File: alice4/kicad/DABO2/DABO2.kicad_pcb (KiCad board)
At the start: 2 copper layers, 74.3 x 117.9 mm, 26 parts, among them J1 POWER, J2 FIRE, J3 HOME, J4 BARTCONN, J5 BLE_DFU, P3 CONN_02X20, P4 CONN_02X07, U1 stmpe811, U2 TFTFRIEND, U3 l3gd20h_breakout, U4 powerboost1000c, U5 bluefruit_le_spi

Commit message: first draft of layout
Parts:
- removed P4: CONN_02X07, DIH_2x7x2mm:DIH_2x7x2mm
- removed REF** (x2): MountingHole_2-5mm, Mounting_Holes:MountingHole_2-5mm
- added C10: 100nF, Capacitors_SMD:C_1206, F.Cu at (171.9, 92.4)
- added C11: 10nF, Capacitors_SMD:C_1206, F.Cu at (168.8, 84.8)
- added C12: 2.2uF, Capacitors_SMD:C_1206, F.Cu at (112.4, 96.6)
- added C13: 100nF, Capacitors_SMD:C_1206, F.Cu at (166.8, 90.3)
- added C14: 100uF, Capacitors_SMD:C_1206, F.Cu at (112.3, 93.6)
- added C15: 10uF, Capacitors_SMD:C_1206, F.Cu at (166.8, 87.9)
- added C16: 10uF, Capacitors_SMD:C_1206, F.Cu at (126.6, 108.2)
- added C17: .1uF, Capacitors_SMD:C_1206, F.Cu at (126.5, 105.7)
- added C18: 10uF, Capacitors_SMD:C_1206, F.Cu at (110.9, 85.0)
- added C6: 10uF, Capacitors_SMD:C_1206, F.Cu at (154.5, 104.9)
- added C7: 1uF, Capacitors_SMD:C_1206, F.Cu at (156.9, 94.1)
- added C8: 1uF, Capacitors_SMD:C_1206, F.Cu at (160.0, 94.1)
- added C9: .1uF, Capacitors_SMD:C_1206, F.Cu at (146.2, 97.9)
- added D1: MBR0540, Diodes_SMD:D_SOD-123, F.Cu at (154.1, 94.3)
- added D2: MM3Z24VT1G, Diodes_SMD:D_SOD-123, F.Cu at (150.3, 97.1)
- added J6: +50mA, Connectors:GS2, B.Cu at (135.1, 97.8)
- added J7: 5VOUT, Pin_Headers:Pin_Header_Straight_1x02_Pitch2.54mm, F.Cu at (107.6, 93.3)
- added J8: PWRSW, Connectors_JST:JST_PH_S2B-PH-SM4-TB_02x2.00mm_Angled, F.Cu at (181.9, 86.4)
- added J9: 5VIN, Pin_Headers:Pin_Header_Straight_1x02_Pitch2.54mm, F.Cu at (107.7, 83.6)
- added L1: 10uH, Resistors_SMD:R_1210, F.Cu at (156.2, 100.9)
- added L2: 6.8uH, Inductors_SMD:L_0402, F.Cu at (119.5, 102.2)
- added R10: 2.2K, Resistors_SMD:R_1206, F.Cu at (173.3, 117.4)
- added R11: 2.2K, Resistors_SMD:R_1206, F.Cu at (173.4, 113.3)
- added R14: 1.87M, Resistors_SMD:R_1206, F.Cu at (121.2, 95.0)
- added R15: 200K, Resistors_SMD:R_1206, F.Cu at (126.4, 95.0)
- added R16: 10K, Resistors_SMD:R_1206, F.Cu at (129.5, 100.5)
- added R17: 10K, Resistors_SMD:R_1206, F.Cu at (172.4, 105.7)
- added R6: 12, Resistors_SMD:R_1206, F.Cu at (140.1, 105.7)
- added R7: 12, Resistors_SMD:R_1206, F.Cu at (140.2, 101.8)
- added R8: 6, Resistors_SMD:R_1206, F.Cu at (140.1, 97.8)
- added R9: 1K, Resistors_SMD:R_1206, F.Cu at (109.9, 100.8)
- added TH1: 15K, Resistors_SMD:R_1206, F.Cu at (169.2, 117.6)
- C1, C2, C3, C4, C5: footprint Capacitors_SMD:C_1206_HandSoldering -> Capacitors_SMD:C_1206
- J1: value POWER -> LIPO; footprint Pin_Headers:Pin_Header_Straight_1x02 -> Connectors_JST:JST_PH_S2B-PH-SM4-TB_02x2.00mm_Angled
- J2: value FIRE -> CONN_01X40; footprint Pin_Headers:Pin_Header_Straight_1x02 -> kyocera_6288:kyocera_6288; moved to B.Cu
- J3: footprint Pin_Headers:Pin_Header_Straight_1x02 -> Connectors_JST:JST_PH_S2B-PH-SM4-TB_02x2.00mm_Angled
- J4: value BARTCONN -> +25mA; footprint Pin_Headers:Pin_Header_Straight_1x05 -> Connectors:GS2; moved to B.Cu
- J5: value BLE_DFU -> +25mA; footprint Pin_Headers:Pin_Header_Straight_1x02 -> Connectors:GS2; moved to B.Cu
- P3: value CONN_02X20 -> GPIO0; footprint Pin_Headers:Pin_Header_Straight_2x20 -> Pin_Headers:Pin_Header_Straight_2x20_Pitch2.54mm; moved to B.Cu
- R1: value 50K -> 10K; footprint Resistors_SMD:R_1206_HandSoldering -> Resistors_SMD:R_1206
- R2: value 10K -> 330K; footprint Resistors_SMD:R_1206_HandSoldering -> Resistors_SMD:R_1206
- R3: value 50K -> 12; footprint Resistors_SMD:R_1206_HandSoldering -> Resistors_SMD:R_1206
- R4: value 10K -> 110K; footprint Resistors_SMD:R_1206_HandSoldering -> Resistors_SMD:R_1206
- R5: value 10K -> 100K; footprint Resistors_SMD:R_1206_HandSoldering -> Resistors_SMD:R_1206
- U2: value TFTFRIEND -> l3gd20h; footprint DIP40:DIP-40_1_ELL -> l3gd20h:l3gd20h
- U3: value l3gd20h_breakout -> mcp73871; footprint L3GD20H:l3gd20h -> Housings_DFN_QFN:QFN-20-1EP_4x4mm_Pitch0.5mm
- U4: value powerboost1000c -> tps61090rsar; footprint PowerBoost1000c:powerboost1000c -> Housings_DFN_QFN:QFN-16-1EP_4x4mm_Pitch0.65mm
- U5: value bluefruit_le_spi -> fan5333bsx; footprint Bluefruit LE SPI:bluefruit_le_spi -> TO_SOT_Packages_SMD:SOT-23-5
- moved J3 88.6 mm to (195.4, 107.5)
- moved HOLE0 73.6 mm to (107.7, 116.4), turned to 270 degrees
- moved U2 69.9 mm to (171.3, 88.1), turned to 90 degrees
- moved P3 62.6 mm to (116.9, 115.5), turned to 270 degrees
- moved HOLE1 57.0 mm to (197.3, 116.4), turned to 270 degrees
- moved U1 56.6 mm to (168.3, 104.0), turned to 0 degrees
- moved C3 55.5 mm to (171.3, 100.0), turned to 0 degrees
- moved C1 55.4 mm to (166.5, 108.2), turned to 180 degrees
- moved R4 53.8 mm to (113.0, 111.3)
- moved C4 53.7 mm to (166.2, 100.0)
- moved J2 46.7 mm to (136.1, 83.8), turned to 0 degrees
- moved R5 46.1 mm to (114.5, 100.9)
- moved C5 41.5 mm to (130.2, 112.0), turned to 0 degrees
- moved J1 39.9 mm to (117.2, 86.7), turned to 180 degrees
- moved R1 35.8 mm to (150.3, 106.7), turned to 270 degrees
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- renumbered REF** to HOLE0, REF** to HOLE1
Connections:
- J1 pad 1: PWREN -> LIPO
- J2 pad 1: FIRE -> LED-K
- J2 pad 2: +3V3 -> LED-A
- J3 pad 1: HOME -> HOME0
- J3 pad 2: +3V3 -> HOME1
- J4 pad 1: GND -> Net-(J4-Pad1)
- J4 pad 2: +3V3 -> GND
- J5 pad 1: BLE_DFU -> Net-(J5-Pad1)
- P3 pad 11: +5V -> Net-(P3-Pad11)
- P3 pad 24: HOME -> HSYNC
- P3 pad 26: FIRE -> VSYNC
- P3 pad 34: BLE_RST -> Net-(P3-Pad34)
- P3 pad 36: AUDIOL_PWM -> HOME0
- P3 pad 37: BLE_IRQ -> Net-(P3-Pad37)
- P3 pad 38: AUDIOR_PWM -> HOME1
- R1 pad 1: GND -> BACKLIGHT_PWM
- R1 pad 2: FIRE -> +3V3
- R2 pad 1: GND -> Net-(R2-Pad1)
- R2 pad 2: HOME -> VJACK
- R3 pad 1: BLE_DFU -> GND
- R3 pad 2: +3V3 -> LED-K
- R4 pad 2: SDA -> Net-(R2-Pad1)
- R5 pad 2: SCL -> Net-(R5-Pad2)
- U1 pad 1: Y- -> YD
- U1 pad 11: Net-(U1-Pad11) -> REGULATED5V
- U1 pad 12: Net-(U1-Pad12) -> GND
- U1 pad 13: X+ -> XL
- U1 pad 15: Y+ -> YU
- U1 pad 16: X- -> XR
- U1 pad 8: HOME -> LIPO
- U1 pad 9: FIRE -> Net-(R17-Pad2)
- U2 pad 1: R0 -> +3V3
- U2 pad 10: B1 -> GND
- U2 pad 11: B2 -> GND
- U2 pad 12: B3 -> GND
- U2 pad 13: B4 -> GND
- U2 pad 14: B5 -> Net-(C11-Pad1)
- U2 pad 15: B6 -> +3V3
- U2 pad 16: B7 -> +3V3
- U2 pad 2: R1 -> SCL
- U2 pad 3: R2 -> SDA
- U2 pad 4: R3 -> GND
- U2 pad 5: R4 -> +3V3
- U2 pad 6: R5 -> Net-(U2-Pad6)
- U2 pad 7: R6 -> Net-(U2-Pad7)
- U2 pad 8: R7 -> GND
- U2 pad 9: B0 -> GND
- U3 pad 1: SCL -> VBAT
- U3 pad 2: SDA -> Net-(R2-Pad1)
- U3 pad 3: GND -> VJACK
- U3 pad 4: +3V3 -> VJACK
- U3 pad 7: GND -> Net-(U3-Pad7)
- U3 pad 8: +3V3 -> Net-(U3-Pad8)
- U3 pad 9: Net-(U3-Pad9) -> VJACK
- U4 pad 1: Net-(U4-Pad1) -> REGULATED5V
- U4 pad 3: Net-(U4-Pad3) -> Net-(L2-Pad2)
- U4 pad 4: PWREN -> Net-(L2-Pad2)
- U4 pad 6: Net-(U4-Pad6) -> GND
- U4 pad 8: Net-(U4-Pad8) -> VBAT
- U5 pad 1: SPIM_SCK -> Net-(D1-Pad2)
- U5 pad 2: SPIM_MISO -> GND
- U5 pad 3: SPIM_MOSI -> LED-K
- U5 pad 4: SPIM_SS -> BACKLIGHT_PWM
- U5 pad 5: BLE_IRQ -> +3V3
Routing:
- net (no net): track 0.57 -> 0.00 mm
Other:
- board size 74.3 x 117.9 mm -> 96 x 39 mm
- board text added: "Alice 4 Daughterboard v2 Brad Grantham Lawrence Kesteloot September 2017"
- board text removed: "Alice 4 Daughterboard v2 Brad Grantham May 2017"

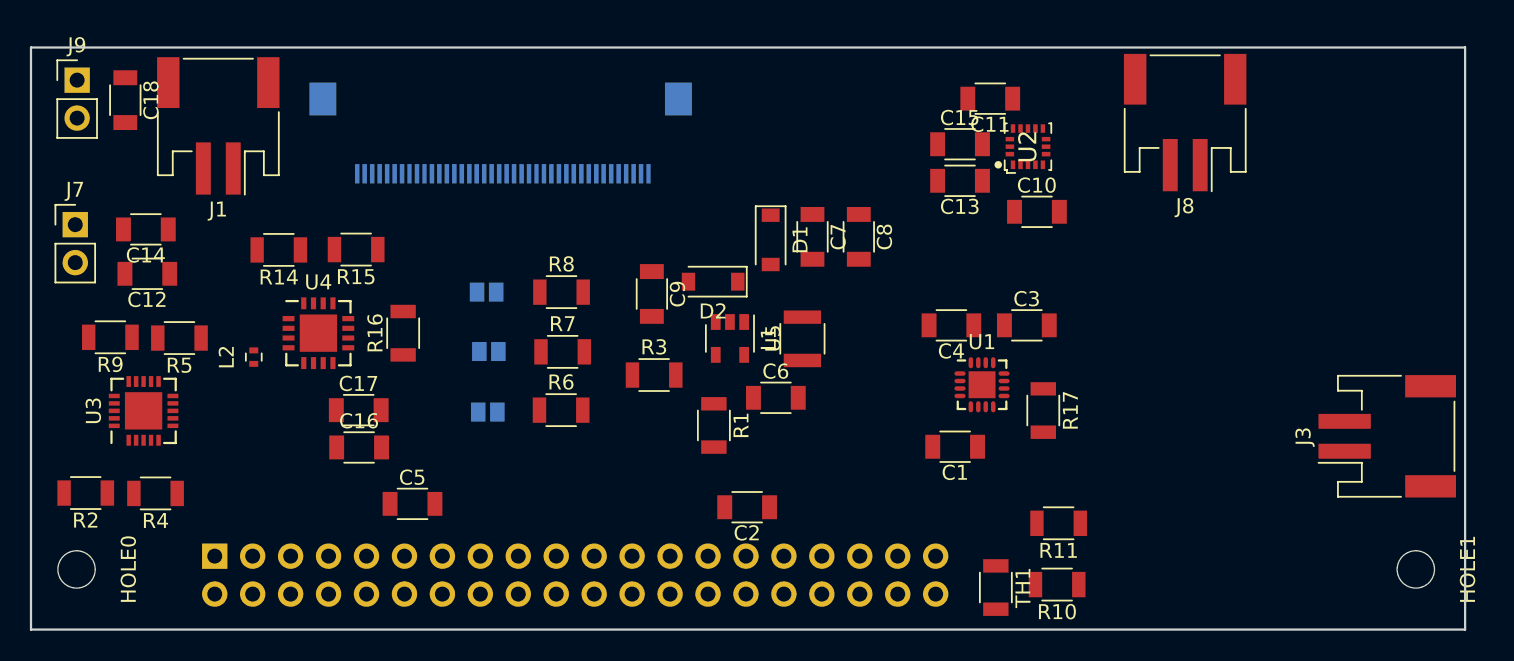
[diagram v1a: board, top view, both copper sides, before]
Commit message: Second draft of layout
Lawrence fixes to schematic

Layout PCB
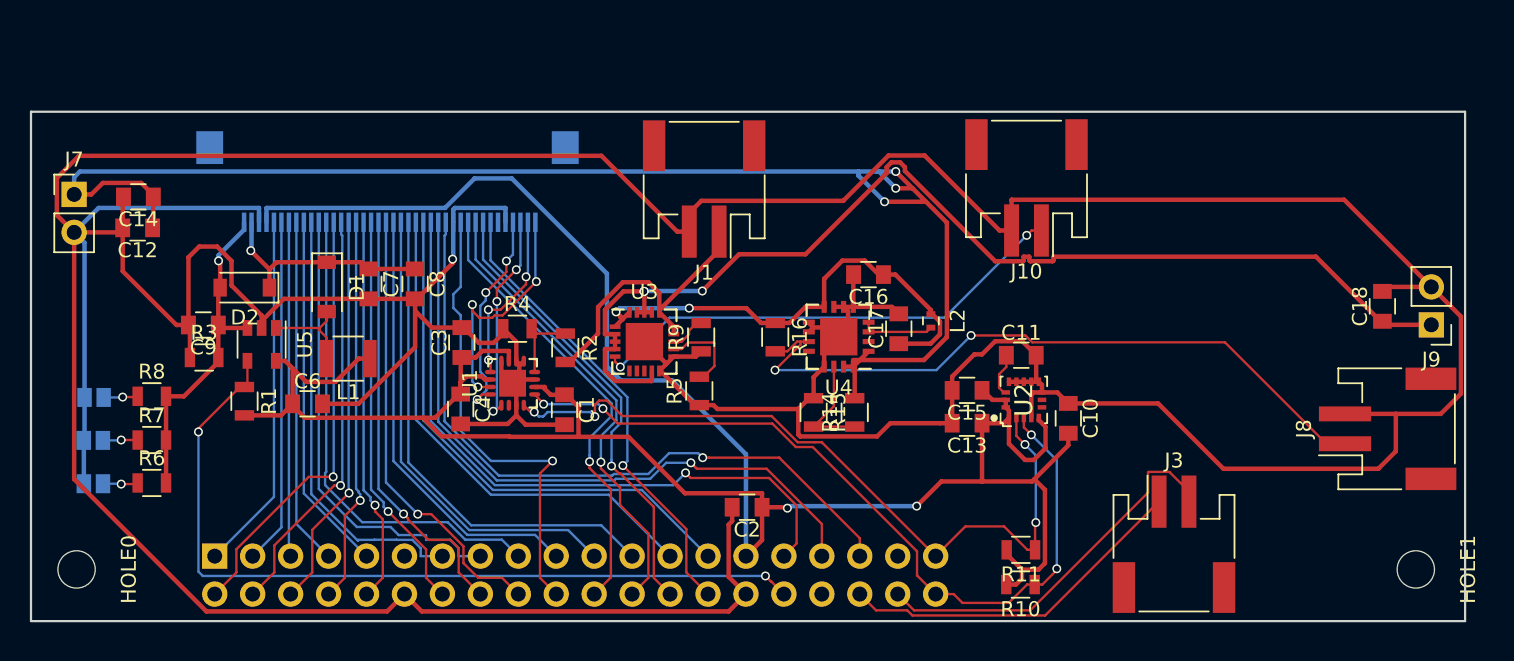
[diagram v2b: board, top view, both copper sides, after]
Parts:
- removed C5: 10uF, Capacitors_SMD:C_1206
- removed R17: 10K, Resistors_SMD:R_1206
- removed TH1: 15K, Resistors_SMD:R_1206
- added J10: THERM, Connectors_JST:JST_PH_S2B-PH-SM4-TB_02x2.00mm_Angled, F.Cu at (171.2, 90.8)
- C1, C10, C11, C12, C13, C14, C15, C16, C17, C18, C2, C3, C4, C6, C7, C8, C9: footprint Capacitors_SMD:C_1206 -> Capacitors_SMD:C_0805
- R1, R10, R11, R14, R15, R16, R3, R5, R6, R7, R8, R9: footprint Resistors_SMD:R_1206 -> Resistors_SMD:R_0805
- R2: value 330K -> 200K; footprint Resistors_SMD:R_1206 -> Resistors_SMD:R_0805
- R4: value 110K -> 200K; footprint Resistors_SMD:R_1206 -> Resistors_SMD:R_0805
- moved J9 92.1 mm to (198.3, 100.0), turned to 180 degrees
- moved C18 85.3 mm to (195.1, 98.8), turned to 90 degrees
- moved L2 45.4 mm to (164.8, 99.7), turned to 270 degrees
- moved R14 40.1 mm to (159.8, 105.8), turned to 90 degrees
- moved R9 39.5 mm to (149.5, 100.8), turned to 90 degrees
- moved C3 37.8 mm to (133.4, 101.2), turned to 90 degrees
- moved C17 36.6 mm to (162.7, 100.2), turned to 90 degrees
- moved C16 36.0 mm to (160.7, 96.6), turned to 180 degrees
- moved R5 35.0 mm to (149.3, 104.4), turned to 90 degrees
- moved U4 34.8 mm to (158.7, 100.8), turned to 180 degrees
- moved U3 33.8 mm to (145.7, 101.1), turned to 0 degrees
- moved R2 33.5 mm to (140.4, 101.5), turned to 270 degrees
- moved C4 33.3 mm to (133.4, 105.6), turned to 270 degrees
- moved J1 32.8 mm to (149.7, 90.9)
- moved R15 32.5 mm to (157.0, 105.8), turned to 270 degrees
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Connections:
- R2 pad 2: VJACK -> LIPO
- U1 pad 11: REGULATED5V -> +3V3
- U1 pad 17: (no net) -> GND
- U1 pad 7: Net-(U1-Pad7) -> GND
- U1 pad 8: LIPO -> Net-(R2-Pad1)
- U1 pad 9: Net-(R17-Pad2) -> GND
- U3 pad 2: Net-(R2-Pad1) -> VJACK
- U3 pad 21: (no net) -> GND
- U4 pad 17: (no net) -> GND
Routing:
- net GND: track 0.00 -> 418.0 mm, vias 0 -> 1
- net +3V3: track 0.00 -> 172.9 mm, vias 0 -> 2
- net REGULATED5V: track 0.00 -> 96.9 mm, vias 0 -> 3
- net VJACK: track 0.00 -> 77.2 mm, vias 0 -> 3
- net BACKLIGHT_PWM: track 0.00 -> 55.5 mm, vias 0 -> 2
- net SDA: track 0.00 -> 53.7 mm, vias 0 -> 4
- net SCL: track 0.00 -> 50.9 mm, vias 0 -> 4
- net PWREN: track 0.00 -> 47.3 mm, vias 0 -> 2
- net B7: track 0.00 -> 46.8 mm, vias 0 -> 1
- net B6: track 0.00 -> 45.0 mm, vias 0 -> 1
- net B5: track 0.00 -> 44.6 mm, vias 0 -> 1
- net B4: track 0.00 -> 36.1 mm
- net B3: track 0.00 -> 34.0 mm
- net B2: track 0.00 -> 33.7 mm
- net Net-(J10-Pad1): track 0.00 -> 32.8 mm, vias 0 -> 2
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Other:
- board size 96 x 39 mm -> 96 x 34.1 mm
- net class Default: clearance 0.2 -> 0.16; trace_width 0.25 -> 0.16
- net class power added: clearance 0.16, trace_width 0.3, via_dia 0.6, via_drill 0.4
- rule trace_clearance: 0.2 -> 0.16
- rule trace_min: 0.2 -> 0.15
- board text added: "DE0-NANO-SOC ARDUINO HEADER"
- board text added: "DE0-NANO-SOC ETHERNET"
- board text added: "DE0-NS 5V JACK"

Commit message: Finish another draft board layout
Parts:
- J7, J9: footprint Pin_Headers:Pin_Header_Straight_1x02_Pitch2.54mm -> Connectors:BARREL_JACK
- J8: footprint Connectors_JST:JST_PH_S2B-PH-SM4-TB_02x2.00mm_Angled -> Connectors_JST:JST_PH_S3B-PH-SM4-TB_03x2.00mm_Angled
- moved J8 86.6 mm to (110.4, 90.9), turned to 180 degrees
- moved J7 80.5 mm to (186.7, 105.2), turned to 180 degrees
- moved C14 71.0 mm to (182.1, 101.5), turned to 0 degrees
- moved C12 70.7 mm to (182.2, 99.4), turned to 0 degrees
- moved C18 14.6 mm to (182.7, 91.0)
- moved J9 13.7 mm to (186.7, 92.8)
- moved J3 1.71 mm to (179.4, 114.5)
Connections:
- HOLE0 pad 1: (no net) -> GND
- HOLE1 pad 1: (no net) -> GND
- J3 pad 1: HOME0 -> HOME1
- J3 pad 2: HOME1 -> HOME0
- J8 pad 1: PWREN -> GND
- J8 pad 2: GND -> PWREN
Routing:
- net REGULATED5V: track 96.9 -> 36.0 mm, vias 3 -> 0
- net VBAT: track 32.8 -> 77.4 mm, vias 2 -> 3
- net VJACK: track 77.2 -> 64.5 mm, vias 3 -> 0
- net PWREN: track 47.3 -> 53.0 mm
- net LIPO: track 20.1 -> 24.4 mm, vias 0 -> 2
- net GND: track 418.0 -> 422.0 mm
- net HOME1: track 26.3 -> 22.5 mm
- net +3V3: track 172.9 -> 176.7 mm
- net HOME0: track 23.8 -> 25.1 mm
- net SCL: track 50.9 -> 50.2 mm
- added copper zone on F.Cu, net +3V3
- added copper zone on B.Cu, net GND

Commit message: one more draft layout
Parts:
- removed R16: 10K, Resistors_SMD:R_0805
- moved J8 59.6 mm to (170.0, 90.8)
- moved C10 25.9 mm to (148.1, 107.0), turned to 180 degrees
- moved U2 21.7 mm to (149.4, 104.0), turned to 0 degrees
- moved C13 21.3 mm to (146.7, 101.2)
- moved C11 18.6 mm to (152.3, 103.9), turned to 270 degrees
- moved C15 17.8 mm to (150.0, 100.2), turned to 90 degrees
- moved C16 15.6 mm to (176.1, 98.9)
- moved J10 14.4 mm to (156.8, 90.9)
- moved R10 13.1 mm to (159.3, 111.0), turned to 270 degrees
- moved C17 12.4 mm to (174.9, 102.1)
- moved L2 12.4 mm to (177.1, 101.5)
- moved R14 12.4 mm to (172.0, 107.7)
- moved R15 12.4 mm to (169.2, 107.7)
- moved U4 12.4 mm to (170.9, 102.6)
- moved U3 12.4 mm to (157.9, 102.9)
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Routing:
- net PWREN: track 53.0 -> 11.2 mm
- net GND: track 422.0 -> 456.7 mm, vias 1 -> 17
- net VBAT: track 77.4 -> 42.7 mm, vias 3 -> 2
- net +3V3: track 176.7 -> 151.2 mm, vias 2 -> 0
- net Net-(J10-Pad1): track 32.8 -> 13.4 mm
- net SDA: track 54.1 -> 39.3 mm, vias 4 -> 2
- net REGULATED5V: track 36.0 -> 23.7 mm
- net SCL: track 50.2 -> 38.2 mm, vias 4 -> 3
- net DATA_ENABLE: track 31.2 -> 42.8 mm
- net VSYNC: track 30.7 -> 40.5 mm
- net B3: track 34.0 -> 43.0 mm
- net B4: track 36.1 -> 45.1 mm
- net LED-A: track 15.0 -> 23.2 mm
- net R4: track 24.1 -> 31.7 mm
- net G7: track 30.0 -> 37.6 mm
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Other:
- board text added: "N.B: F.CU (AND PARTS) FACES DE0-NANO-SOC PARTS SIDE"

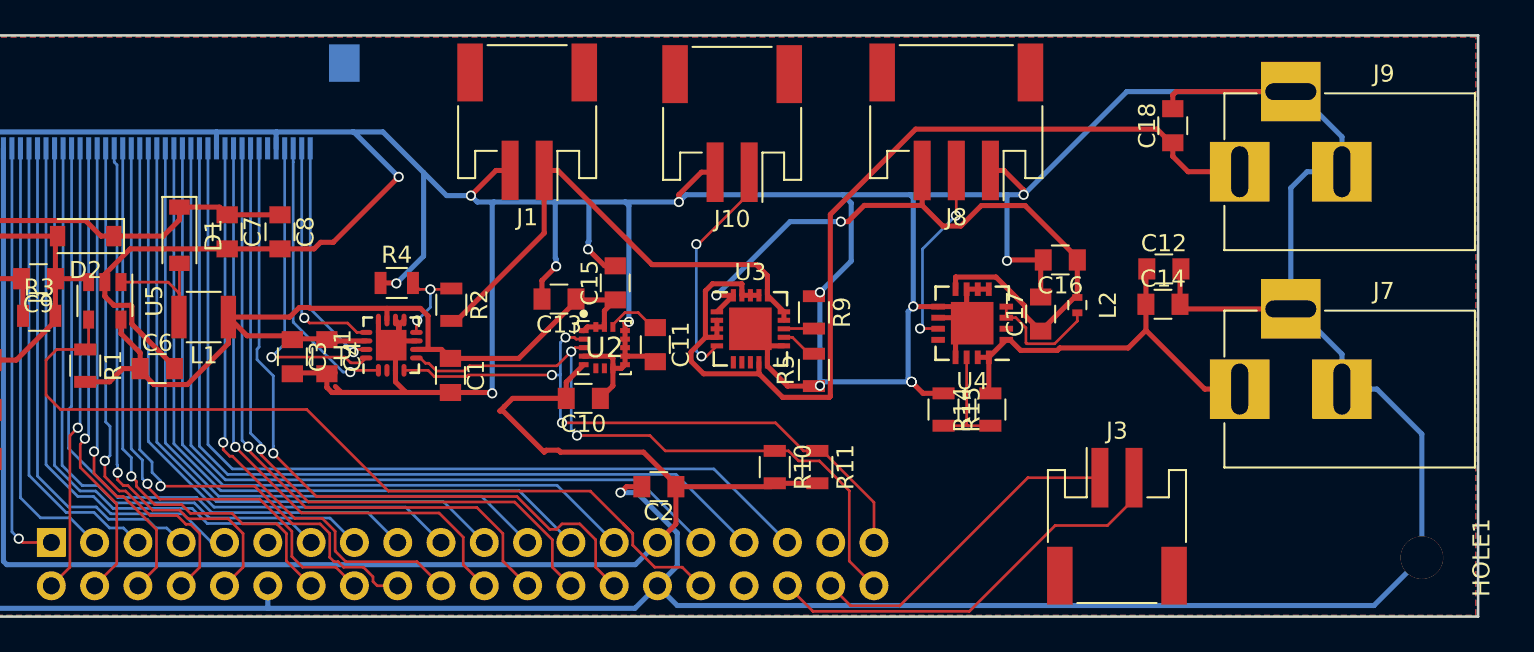
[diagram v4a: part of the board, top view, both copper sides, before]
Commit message: one more draft layout; better 3v3 plane
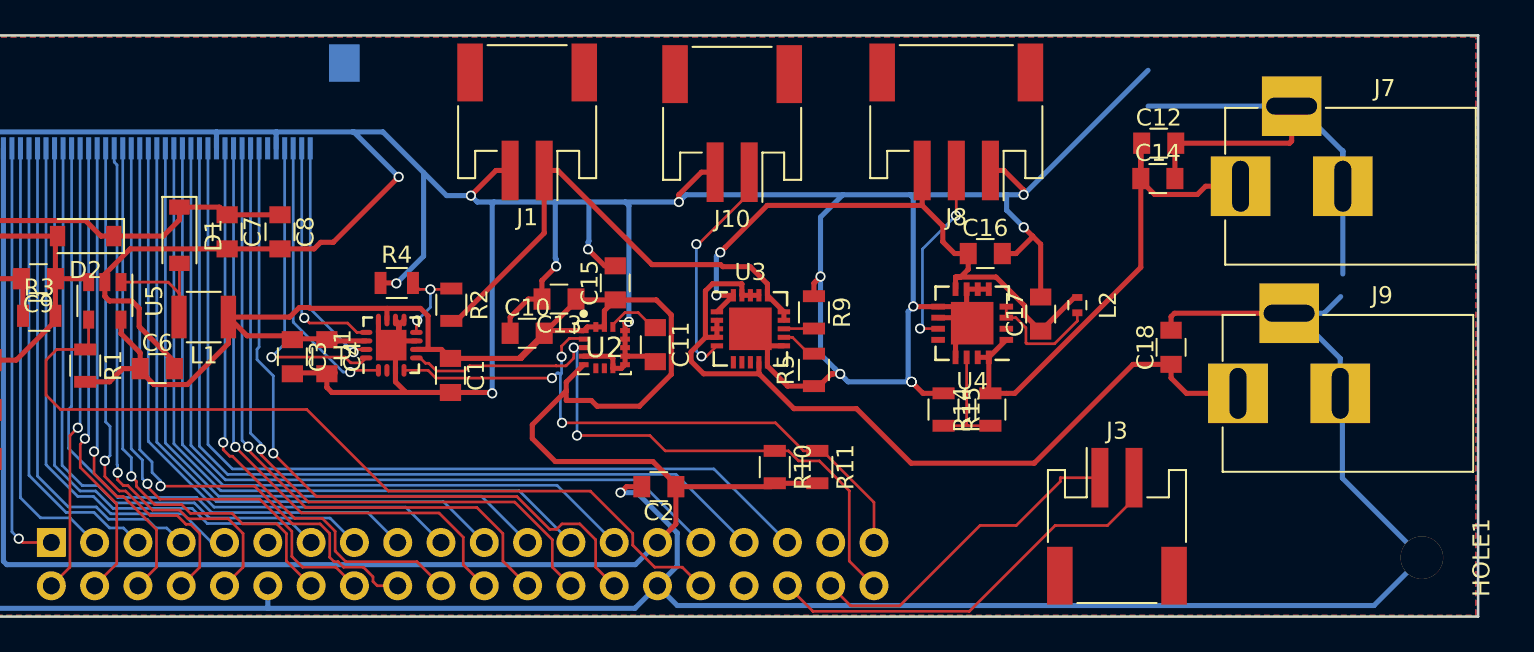
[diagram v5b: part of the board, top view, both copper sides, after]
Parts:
- moved C18 13.0 mm to (182.6, 104.0)
- moved J9 13.0 mm to (186.5, 106.7)
- moved J7 11.9 mm to (186.7, 94.6)
- moved C12 7.38 mm to (181.9, 92.0)
- moved C14 7.38 mm to (181.8, 94.1)
- moved C10 5.04 mm to (144.8, 103.2), turned to 0 degrees
- moved C16 4.42 mm to (171.7, 98.5), turned to 0 degrees
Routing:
- net +3V3: track 151.2 -> 166.7 mm
- net VJACK: track 58.1 -> 49.1 mm
- net REGULATED5V: track 23.7 -> 32.3 mm
- net VBAT: track 42.7 -> 36.6 mm
- net GND: track 456.7 -> 461.9 mm
- net BACKLIGHT_PWM: track 50.7 -> 49.9 mm
- net SDA: track 39.3 -> 39.8 mm

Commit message: Hopefully near final layout
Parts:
- added R12: 22, Resistors_SMD:R_0805, F.Cu at (125.9, 109.9)
- added TP1: GND, testpoint_smd_1206:testpoint_smd_1206, F.Cu at (112.0, 116.1)
- added TP2: 3V3, testpoint_smd_1206:testpoint_smd_1206, F.Cu at (156.3, 112.2)
- added TP3: 5VIN, testpoint_smd_1206:testpoint_smd_1206, F.Cu at (179.2, 107.2)
- added TP4: LED-A, testpoint_smd_1206:testpoint_smd_1206, F.Cu at (110.9, 95.0)
- added TP5: LIPO, testpoint_smd_1206:testpoint_smd_1206, F.Cu at (164.4, 97.5)
- added TP6: 5VOUT, testpoint_smd_1206:testpoint_smd_1206, F.Cu at (178.2, 98.7)
- added TP7: SDA, testpoint_smd_1206:testpoint_smd_1206, F.Cu at (172.4, 112.3)
- added TP8: SCL, testpoint_smd_1206:testpoint_smd_1206, F.Cu at (168.6, 112.3)
- J2: value CONN_01X40 -> LCD
- moved R8 1.60 mm to (112.7, 103.2)
- moved J6 1.60 mm to (108.8, 103.2)
- moved J4 1.13 mm to (108.7, 111.8)
- moved R6 1.13 mm to (112.6, 111.7)
- moved R7 0.20 mm to (112.7, 107.5)
- moved J5 0.20 mm to (108.8, 107.5)
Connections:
- J2 pad 30: LCD_CLK -> Net-(J2-Pad30)
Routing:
- net Net-(J2-Pad30): track 0.00 -> 17.1 mm, vias 0 -> 1
- net LCD_CLK: track 34.5 -> 17.5 mm, vias 1 -> 0
- net SDA: track 39.8 -> 49.4 mm
- net LIPO: track 29.6 -> 36.3 mm
- net LED-A: track 23.2 -> 27.8 mm
- net GND: track 461.9 -> 465.8 mm
- net SCL: track 38.2 -> 41.9 mm
- net VJACK: track 49.1 -> 52.3 mm
- net REGULATED5V: track 32.3 -> 35.2 mm
- net LED-K: track 27.3 -> 30.1 mm
- net BACKLIGHT_PWM: track 49.9 -> 49.4 mm
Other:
- board text added: "+24V"
- board text added: "+25mA"
- board text added: "+50mA"
- board text added: "3V3"
- board text added: "Alice 4 Project DE0-Nano-SoC/DE10-Nano Peripheral V1 Brad Grantham, Lawrence Kesteloot September 2017"
- board text added: "GND"
- board text added: "REG5V"
- board text added: "SCL"
- board text added: "SDA"
- board text added: "VJACK"
- board text removed: "Alice 4 Daughterboard v2 Brad Grantham Lawrence Kesteloot September 2017"
